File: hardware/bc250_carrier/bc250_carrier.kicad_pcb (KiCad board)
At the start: 2 copper layers, 80 x 55 mm, 15 parts, among them J1 PSU Mini-Fit Jr 2x5, J10 SENSE, J3 STRIP, J5 FAN1 GPIO5, J6 FAN2 GPIO6, J7 FAN3 GPIO7, J8 FAN4 GPIO10, J9 BTN, Q1 2N7000, U1 ESP32-C3 Super Mini

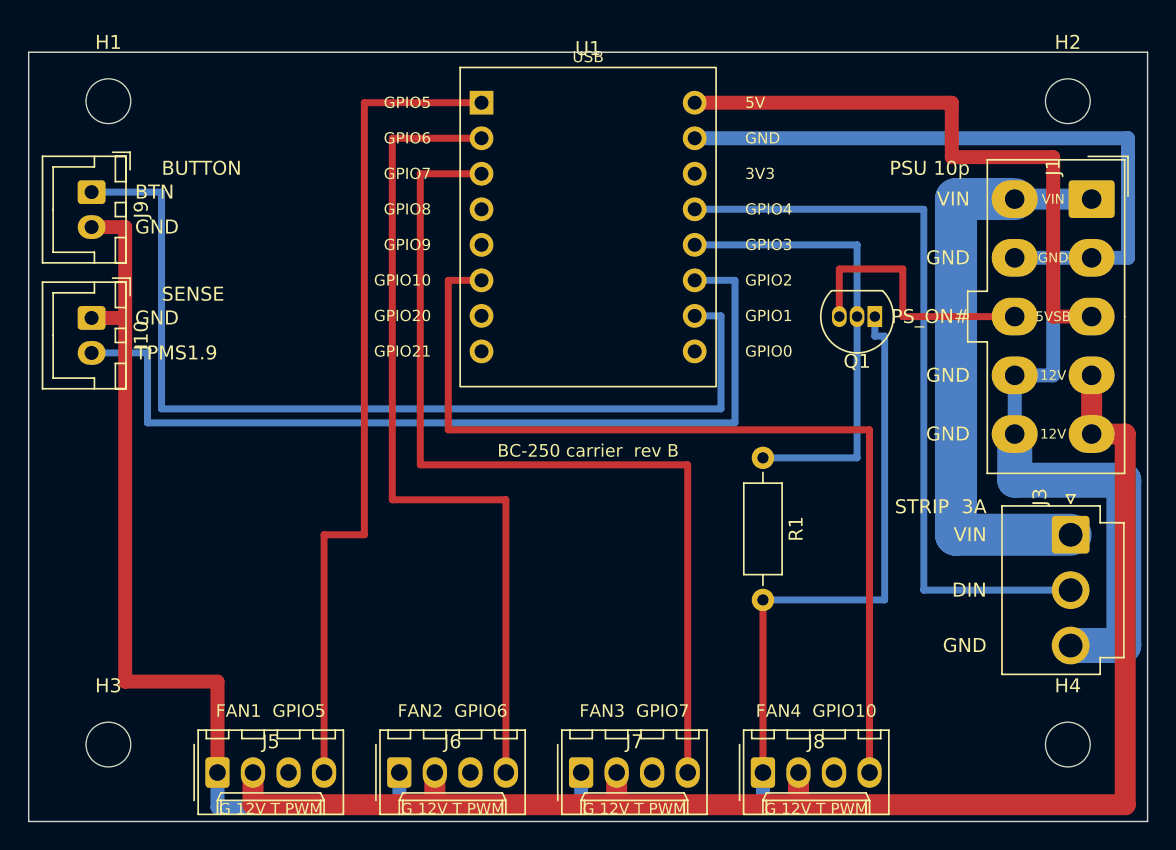
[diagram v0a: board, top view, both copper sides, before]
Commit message: hardware: BC-250 carrier rev C — right-angle PSU header, J11 breakout, wider rails
Rev C relays the 80 x 34.5 mm board around a RIGHT-ANGLE Mini-Fit Jr
(DLL-5569-10AW, C22365658) on the bottom edge: the PSU plug lies flat over a
tracks-only "plug zone" and its wires leave over the top edge.  The 3.3 V
strip feed is a 3 mm track, its return 2.5 mm.  New optional 2x8 breakout
header J11 along the left edge carries 3.3V, 5VSB and 12 V on two pins each
plus every unused GPIO (8, 9, 20, 21, 0) with a ground beside it.  The
button J9 grows to 4 pins (12 V + GND for its ring LED), the sense connector
shrinks to a single pin, the fan headers become a 2 x 2 block spaced for real
fan plugs (Ckmtw W-2510S04P, C140769 — C41927 was a shrouded wafer a fan plug
cannot enter), R1 moves to 7.62 mm pitch, GATE hops layers through two vias.

Every LCSC part number was re-verified against LCSC's product API; MOQs and
pin headers (C2337, C124382) fixed.  `make` now runs KiCad's real DRC through
the pcbnew Python module (drc.py; only the two stock-M3-courtyard overlaps are
tolerated) alongside check.py, and `make preview` renders a quick Pillow PNG.

The J11 rails were then widened so the breakout is good for about 2 A each,
not the 1.3-1.6 A its 0.5-0.6 mm tracks allowed: 12 V 1.2 mm (back layer up
the strip between J11 and the module), 5VSB 1.0 mm (front layer, same strip;
its trunk from the header to the module 1.0 -> 1.5 mm since J11's draw flows
through it), 3.3V 0.9 mm — the most that fits between mounting holes H3/H1 and
the board edge under the 0.25 hole / 0.3 edge rules.  The README gains a
current budget: the fan block's split 12 V feed is ~2.7 A per column, enough
for a fan plus an AIO pump.

Still to confirm on hardware: the PSU pin map, the module's orientation, and
fan plug polarity.
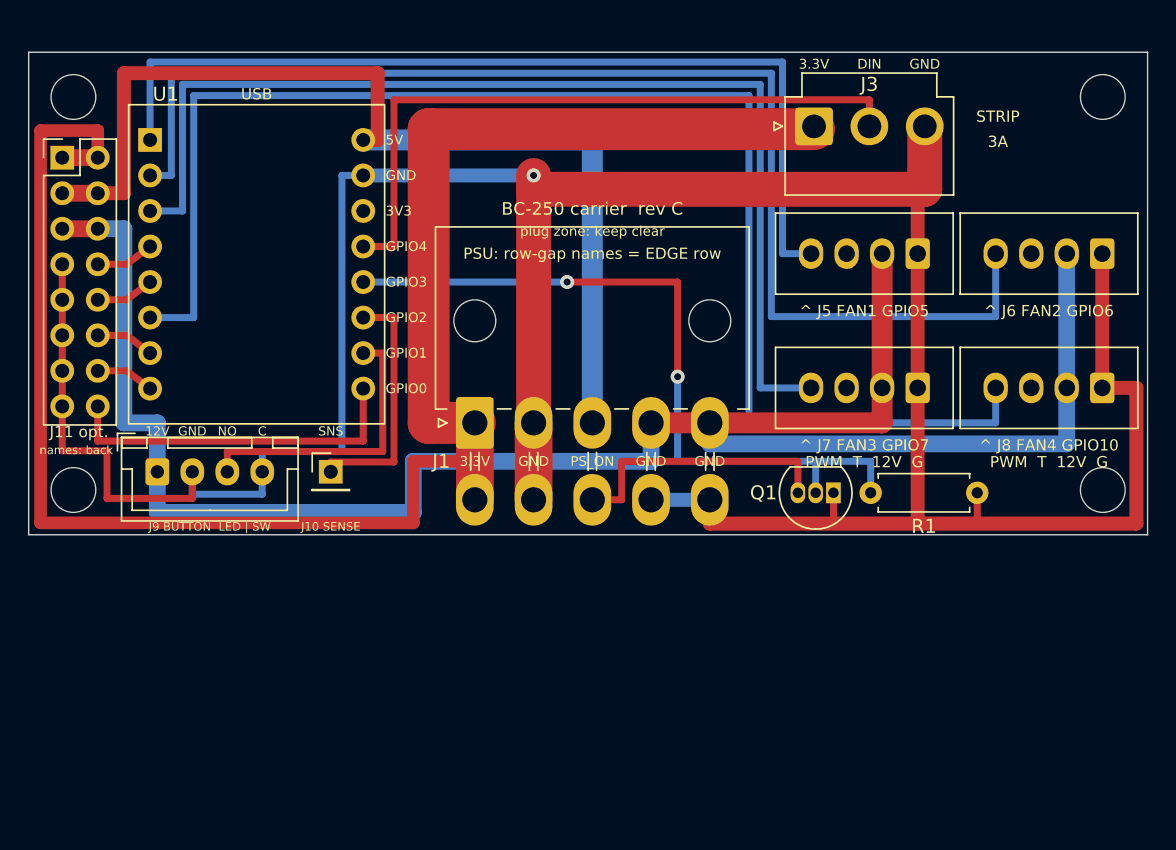
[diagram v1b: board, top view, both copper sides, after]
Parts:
- added J11: PWR+GPIO/GND (optional), Connector_PinHeader_2.54mm:PinHeader_2x08_P2.54mm_Vertical, F.Cu at (102.4, 107.5)
- J1: value PSU Mini-Fit Jr 2x5 -> PSU Mini-Fit Jr 2x5 R/A; footprint Connector_Molex:Molex_Mini-Fit_Jr_5566-10A_2x05_P4.20mm_Vertical -> Connector_Molex:Molex_Mini-Fit_Jr_5569-10A2_2x05_P4.20mm_Horizontal
- J10: footprint Connector_JST:JST_XH_B2B-XH-A_1x02_P2.50mm_Vertical -> Connector_PinHeader_2.54mm:PinHeader_1x01_P2.54mm_Vertical
- J9: value BTN -> BUTTON; footprint Connector_JST:JST_XH_B2B-XH-A_1x02_P2.50mm_Vertical -> Connector_JST:JST_XH_B4B-XH-A_1x04_P2.50mm_Vertical
- R1: footprint Resistor_THT:R_Axial_DIN0207_L6.3mm_D2.5mm_P10.16mm_Horizontal -> Resistor_THT:R_Axial_DIN0207_L6.3mm_D2.5mm_P7.62mm_Horizontal
- moved J6 62.5 mm to (176.8, 114.4), turned to 180 degrees
- moved J5 62.3 mm to (163.6, 114.4), turned to 180 degrees
- moved J1 46.9 mm to (131.9, 126.5), turned to 0 degrees
- moved J8 36.7 mm to (176.8, 124.0), turned to 180 degrees
- moved J7 36.5 mm to (163.6, 124.0), turned to 180 degrees
- moved J3 34.5 mm to (156.2, 105.3), turned to 0 degrees
- moved U1 23.8 mm to (116.3, 115.2)
- moved J9 20.5 mm to (109.2, 130.0), turned to 0 degrees
- moved J10 20.3 mm to (121.6, 130.0), turned to 0 degrees
- moved H3 18.4 mm to (103.2, 131.3)
- moved H4 18.4 mm to (176.8, 131.3)
- moved Q1 12.9 mm to (157.5, 131.5)
- moved R1 8.10 mm to (160.2, 131.5), turned to 0 degrees
- moved H1 2.52 mm to (103.2, 103.2)
- moved H2 2.52 mm to (176.8, 103.2)
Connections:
- net VIN renamed 3.3V
- J10 pad 1: GND -> SENSE
- J9 pad 1: BTN -> 12V
- U1 pad 16: (no net) -> GPIO0
- U1 pad 4: (no net) -> GPIO8
- U1 pad 5: (no net) -> GPIO9
- U1 pad 7: (no net) -> GPIO20
- U1 pad 8: (no net) -> GPIO21
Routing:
- net 3.3V: track 41.9 -> 129.4 mm
- net GND: track 268.5 -> 218.8 mm, vias 0 -> 1
- net BTN: track 69.0 -> 21.0 mm
- net SENSE: track 64.1 -> 17.8 mm
- net FAN_GPIO10: track 67.7 -> 102.2 mm
- net 12V: track 104.7 -> 138.0 mm
- net 5VSB: track 43.7 -> 73.5 mm
- net FAN_GPIO6: track 59.8 -> 89.7 mm
- net GPIO0: track 0.00 -> 25.2 mm
- net GATE: track 33.6 -> 53.6 mm, vias 0 -> 2
- net FAN_GPIO7: track 66.3 -> 78.0 mm
- net FAN_GPIO5: track 59.1 -> 66.5 mm
- net DIN: track 54.1 -> 48.6 mm
- net GPIO20: track 0.00 -> 4.17 mm
- net GPIO9: track 0.00 -> 4.17 mm
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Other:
- board size 80 x 55 mm -> 80 x 34.5 mm
- board text added: "2x 12V"
- board text added: "2x 3.3V"
- board text added: "2x 5VSB"
- board text added: "3.3V"
- board text added: "3A"
- board text added: "BC-250 carrier rev C"
- board text added: "C"
- board text added: "GPIO0"
- board text added: "GPIO20"
- board text added: "GPIO21"
- board text added: "GPIO8"
- board text added: "GPIO9"
- board text added: "J10 SENSE"
- board text added: "J11 opt."
- board text added: "J11: GND beside each GPIO"
- board text added: "J9 BUTTON LED | SW"
- board text added: "NO"
- board text added: "PSU: row-gap names = EDGE row"
- board text added: "PSU: row-gap names = INNER row"
- board text added: "PS_ON"
- board text added: "PWM T 12V G"
- board text added: "SNS"
- board text added: "STRIP"
- board text added: "^ J5 FAN1 GPIO5"
- board text added: "^ J6 FAN2 GPIO6"
- board text added: "^ J7 FAN3 GPIO7"
- board text added: "^ J8 FAN4 GPIO10"
- board text added: "names: back"
- board text added: "plug zone: keep clear"
- board text added: "serial_led_controller"
- board text removed: "BC-250 carrier rev B"
- board text removed: "BTN"
- board text removed: "BUTTON"
- board text removed: "FAN1 GPIO5"
- board text removed: "FAN2 GPIO6"
- board text removed: "FAN3 GPIO7"
- board text removed: "FAN4 GPIO10"
- board text removed: "G 12V T PWM"
- board text removed: "PSU 10p"
- board text removed: "PS_ON#"
- board text removed: "SENSE"
- board text removed: "STRIP 3A"
- board text removed: "TPMS1.9"
- board text removed: "VIN"
- board text removed: "serial_led_controller BC-250 carrier rev B"

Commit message: carrier pcb: order-ready assembly files per fab, the Super Mini plugs into sockets
fab.py turns the exported gerbers, position file and generate.py's parts
tables into one folder per fab under out/fab/ (JLCPCB, PCBWay): gerber zip,
BOM and pick-and-place in that fab's own column layout, driven by a PROVIDERS
table so another fab is one more entry. `make export` runs it.

The ESP32-C3 Super Mini is no longer soldered: it plugs into two 1x8 5.7 mm
low-profile female headers (J12/J13), so an assembled board from either fab
is complete and the module comes out for reflashing. U1 stays schematic-only.
Fan headers are now the Molex 47053-1000 the 4-wire fan spec names (the
Ckmtw ramp had to be cut for the plug's latch wall), J10/J11 move to stocked
LCSC parts, and the README gains an Ordering section covering assembled and
self-soldered routes.
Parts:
- removed U1: ESP32-C3 Super Mini, bc250_carrier:ESP32-C3_SuperMini
- added J12: U1 socket L, Connector_PinSocket_2.54mm:PinSocket_1x08_P2.54mm_Vertical, F.Cu at (108.7, 106.3)
- added J13: U1 socket R, Connector_PinSocket_2.54mm:PinSocket_1x08_P2.54mm_Vertical, F.Cu at (123.9, 106.3)
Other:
- board text added: "3V3"
- board text added: "5V"
- board text added: "GPIO1"
- board text added: "GPIO2"
- board text added: "GPIO3"
- board text added: "GPIO4"
- board text added: "Super Mini"
- board text added: "U1 ESP32-C3"
- board text added: "USB"
- board text added: "antenna v"
- board text added: "pins down, USB-C ^"
- board text added: "plugs in here"

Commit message: carrier pcb rev D: 0.5 mm hand-solder clearances, wide TO-92, rails split from the GPIOs
Board 2's fault was PS_ON# bridged to GATE at the stock TO-92's 0.3 mm
gate-drain gap; Q1 is now on the wide footprint. check.py holds tracks
0.5 mm from any other part's pad (0.3 track to track), and on the back
12 V passes no 5VSB, GATE or GPIO pad. J11 becomes a 2x6 of SENSE + the
spare GPIOs with GND beside each; the rails move to their own 2x3 J14.
Both layers get a ground fill (fill.py: KiCad's zone filler + stitching
vias).
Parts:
- removed H1: M3, MountingHole:MountingHole_3.2mm_M3
- removed J10: SENSE, Connector_PinHeader_2.54mm:PinHeader_1x01_P2.54mm_Vertical
- added J14: PWR 3.3V/5VSB/12V (optional), Connector_PinHeader_2.54mm:PinHeader_2x03_P2.54mm_Vertical, F.Cu at (102.4, 102.9)
- J11: value PWR+GPIO/GND (optional) -> SENSE+GPIO/GND; footprint Connector_PinHeader_2.54mm:PinHeader_2x08_P2.54mm_Vertical -> Connector_PinHeader_2.54mm:PinHeader_2x06_P2.54mm_Vertical
- Q1: footprint Package_TO_SOT_THT:TO-92_Inline -> Package_TO_SOT_THT:TO-92_Inline_Wide
- moved J11 5.08 mm to (102.4, 112.6)
- moved J9 0.60 mm to (109.2, 130.6)
- moved Q1 0.46 mm to (158.0, 131.5)
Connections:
- J11 pad 1: 3.3V -> GND
- J11 pad 10: GPIO9 -> GPIO21
- J11 pad 12: GPIO20 -> GPIO0
- J11 pad 2: 3.3V -> SENSE
- J11 pad 3: 5VSB -> GND
- J11 pad 4: 5VSB -> GPIO8
- J11 pad 5: 12V -> GND
- J11 pad 6: 12V -> GPIO9
- J11 pad 8: GPIO8 -> GPIO20
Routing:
- net 12V: track 138.0 -> 164.1 mm, vias 0 -> 1
- net SENSE: track 17.8 -> 41.6 mm
- net 5VSB: track 73.5 -> 66.2 mm
- net 3.3V: track 129.4 -> 123.1 mm
- net GND: track 218.8 -> 222.6 mm, vias 1 -> 46
- net PS_ON#: track 19.7 -> 17.4 mm
- net DIN: track 48.6 -> 49.6 mm
- net BTN: track 21.0 -> 22.0 mm
- net GATE: vias 2 -> 1
- added copper zone on B.Cu, net GND
- added copper zone on F.Cu, net GND
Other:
- board text added: "BC-250 carrier rev D"
- board text added: "D"
- board text added: "G"
- board text added: "J11 SNS/IO"
- board text added: "J14 PWR"
- board text added: "S"
- board text added: "SENSE"
- board text removed: "BC-250 carrier rev C"
- board text removed: "J10 SENSE"
- board text removed: "J11 opt."
- board text removed: "SNS"
